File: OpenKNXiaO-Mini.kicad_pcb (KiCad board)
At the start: 4 copper layers, 23 x 30.8 mm, 13 parts, among them J1 Conn_KNX, J5 Conn_01x05, J6 Conn_01x05, J7 Conn_01x12, SW1 Prog BTN, U1 Seeeduino XIAO

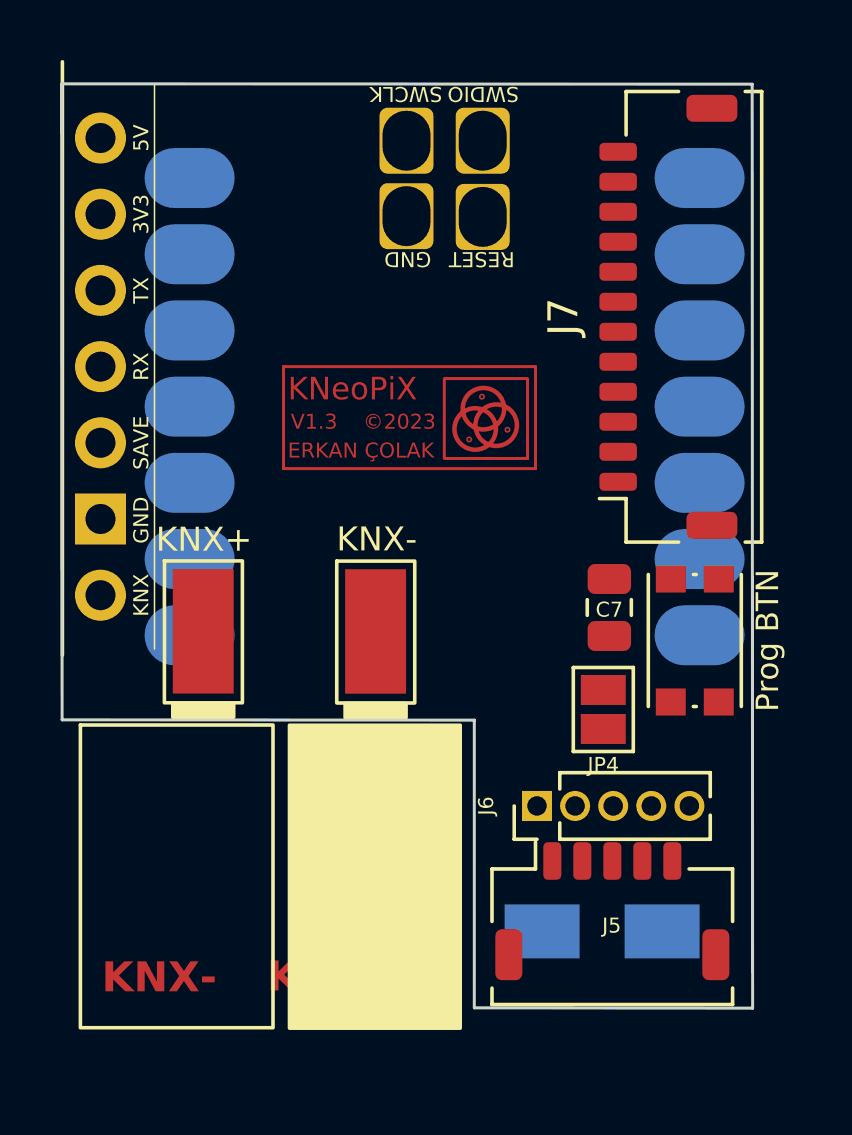
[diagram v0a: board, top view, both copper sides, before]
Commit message: OpenKNXiaO - Final form and dimensions are now established.
Initial housing is startet. Dimensions could be changed later
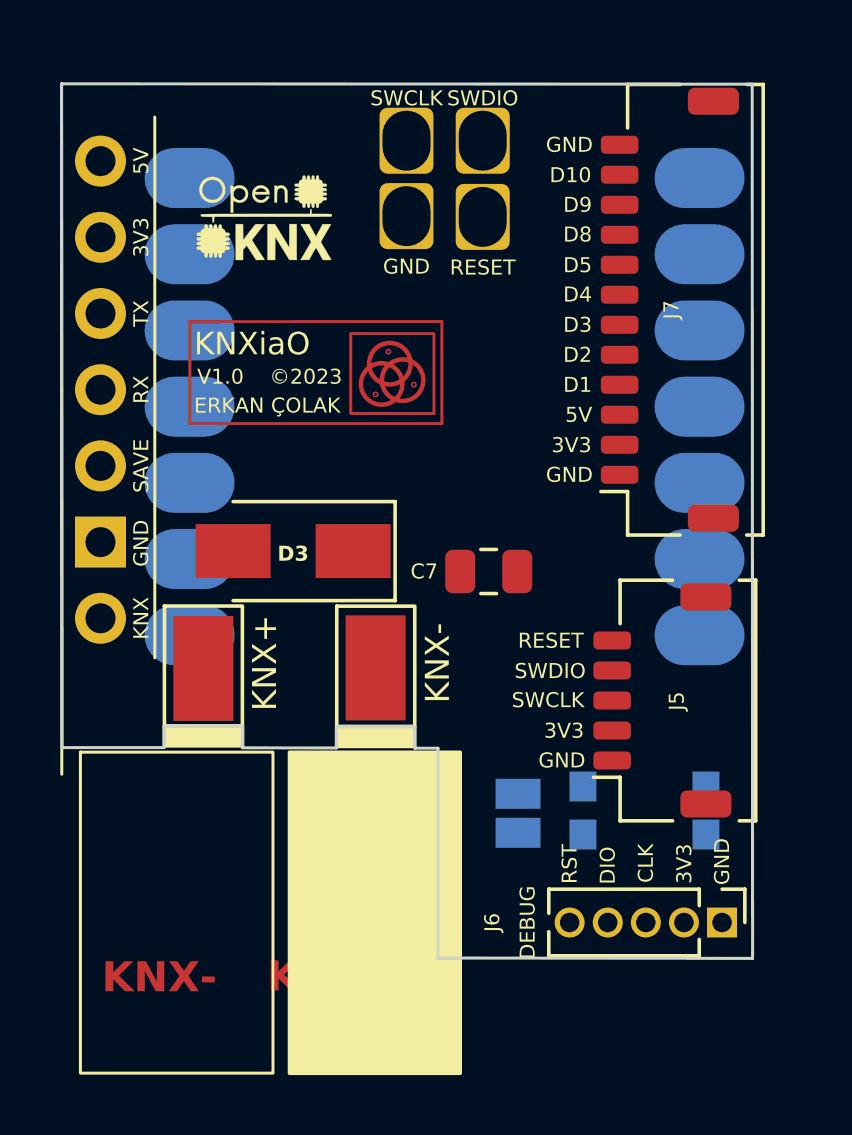
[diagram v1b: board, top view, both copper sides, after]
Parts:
- D3, REF1: moved to F.Cu
- GN1: footprint KNeoPix:NanoBCU_PinSocket_LowProfile -> KNeoPix:OpenKNX_BCU_V2.0
- JP4, SW1: moved to B.Cu
- moved REF1 21.7 mm to (118.6, 104.2), turned to 0 degrees
- moved D3 16.3 mm to (119.6, 115.1)
- moved J6 7.29 mm to (133.9, 127.5), turned to -90 degrees
- moved J5 7.22 mm to (131.9, 120.0), turned to 90 degrees
- moved SW1 5.91 mm to (131.3, 123.7), turned to 0 degrees
- moved JP4 4.48 mm to (127.1, 123.8)
- moved C7 4.20 mm to (126.1, 115.8), turned to 180 degrees
- moved REF42 3.46 mm to (120.2, 108.9)
- moved J1 1.50 mm to (116.6, 117.8)
- moved GN1 0.77 mm to (113.1, 117.3)
- moved J7 0.24 mm to (132.1, 107.0)
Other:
- board size 23 x 30.8 mm -> 23 x 29.2 mm

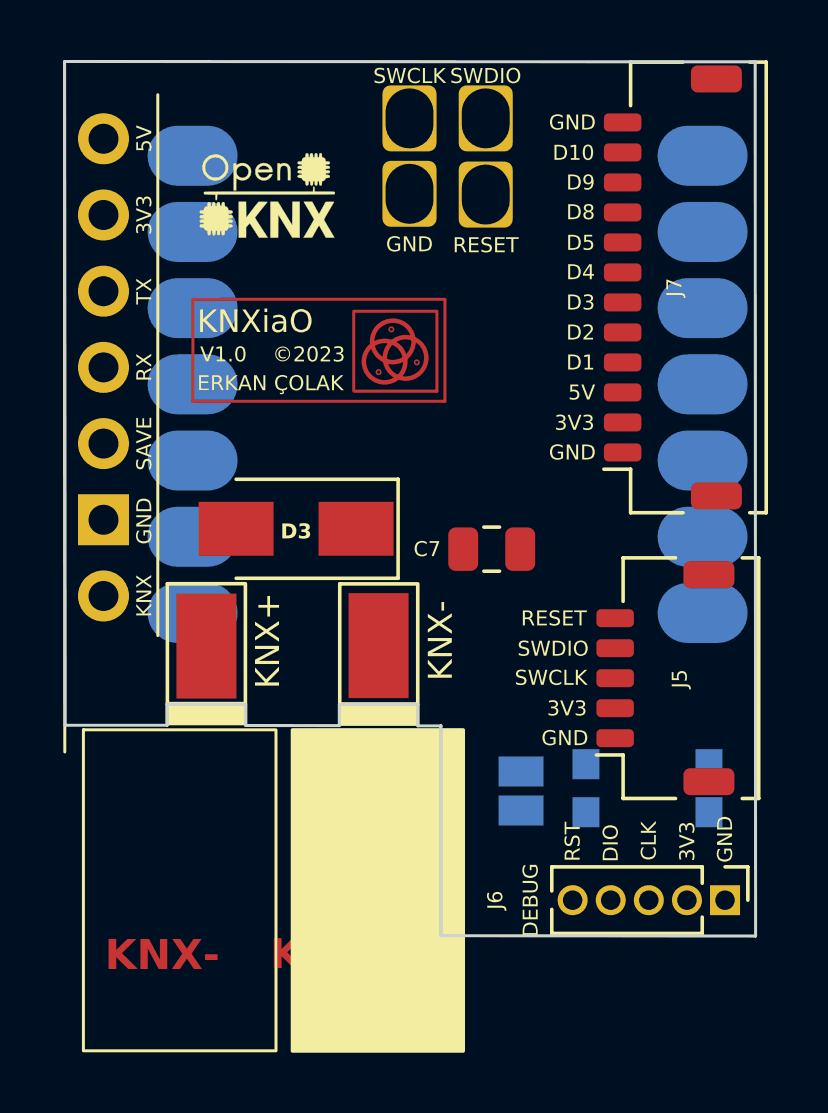
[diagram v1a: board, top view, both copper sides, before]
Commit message: Centered KNX connection and first routing
Updated low high profile (Pin-Header / Low BCU)
Removed SMA Diode. BCU has allready its own.
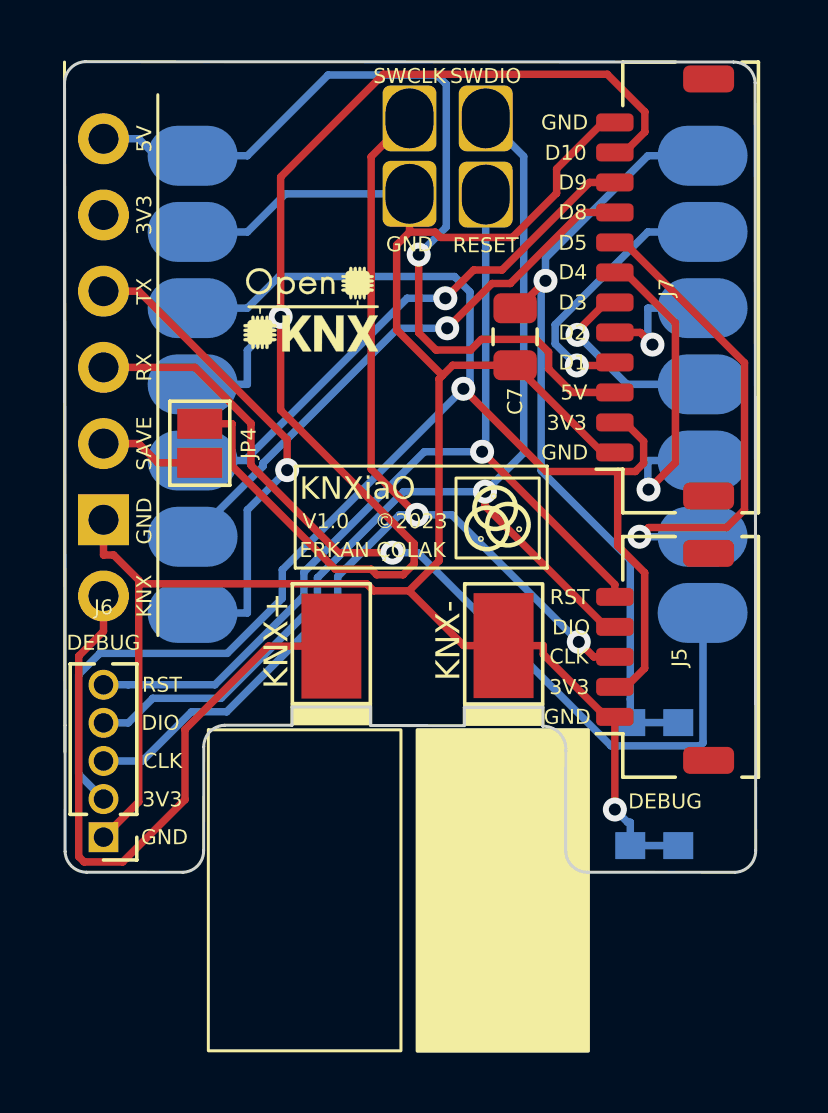
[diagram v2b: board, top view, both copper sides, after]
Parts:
- removed D3: SMAJ40CA-13-F, KNeoPix:D_SMA
- JP4: moved to F.Cu
- moved J6 20.8 mm to (113.1, 125.3), turned to 180 degrees
- moved JP4 15.8 mm to (116.3, 112.2)
- moved C7 7.12 mm to (126.9, 108.7), turned to -90 degrees
- moved REF42 6.52 mm to (123.6, 114.5)
- moved J1 4.17 mm to (120.7, 117.8)
- moved REF1 4.06 mm to (120.1, 108.0)
- moved J5 0.71 mm to (131.9, 119.3)
- moved SW1 0.27 mm to (131.5, 123.6), turned to 90 degrees
- moved J7 0.26 mm to (131.9, 107.0)
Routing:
- net KNX_GND: track 0.00 -> 74.1 mm, vias 0 -> 1
- net S_3V3: track 0.00 -> 52.4 mm, vias 0 -> 1
- net D10: track 0.00 -> 45.5 mm, vias 0 -> 1
- net SWCLK: track 0.00 -> 37.3 mm, vias 0 -> 2
- net SWDIO: track 0.00 -> 36.4 mm, vias 0 -> 1
- net RESET: track 0.00 -> 31.6 mm, vias 0 -> 1
- net KNX_RX: track 0.00 -> 30.4 mm, vias 0 -> 1
- net KNX_5V: track 0.00 -> 29.5 mm, vias 0 -> 1
- net D0: track 0.00 -> 26.4 mm, vias 0 -> 1
- net KNX+: track 0.00 -> 21.9 mm
- net D8: track 0.00 -> 18.6 mm, vias 0 -> 1
- net D9: track 0.00 -> 18.0 mm, vias 0 -> 1
- net D5_SCL: track 0.00 -> 16.9 mm, vias 0 -> 1
- net KNX_TX: track 0.00 -> 16.3 mm, vias 0 -> 1
- net D4_SDA: track 0.00 -> 11.4 mm, vias 0 -> 1
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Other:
- board size 23 x 29.2 mm -> 23 x 27 mm
- copper layers 4 -> 2
- board text removed: "KNX+"
- board text removed: "KNX-"

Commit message: Prog. Move to outside
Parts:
- moved SW1 1.80 mm to (133.3, 123.6)
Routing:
- net KNX+: track 21.9 -> 8.91 mm, vias 0 -> 1
- net KNX_RX: track 30.4 -> 25.0 mm, vias 1 -> 3
- net KNX_GND: track 74.1 -> 76.6 mm
- net RESET: track 31.6 -> 33.4 mm
- net D0: track 26.4 -> 27.8 mm
- net SWDIO: track 36.4 -> 37.7 mm
- net S_3V3: track 52.4 -> 53.7 mm, vias 1 -> 3
- net SWCLK: track 37.3 -> 38.2 mm

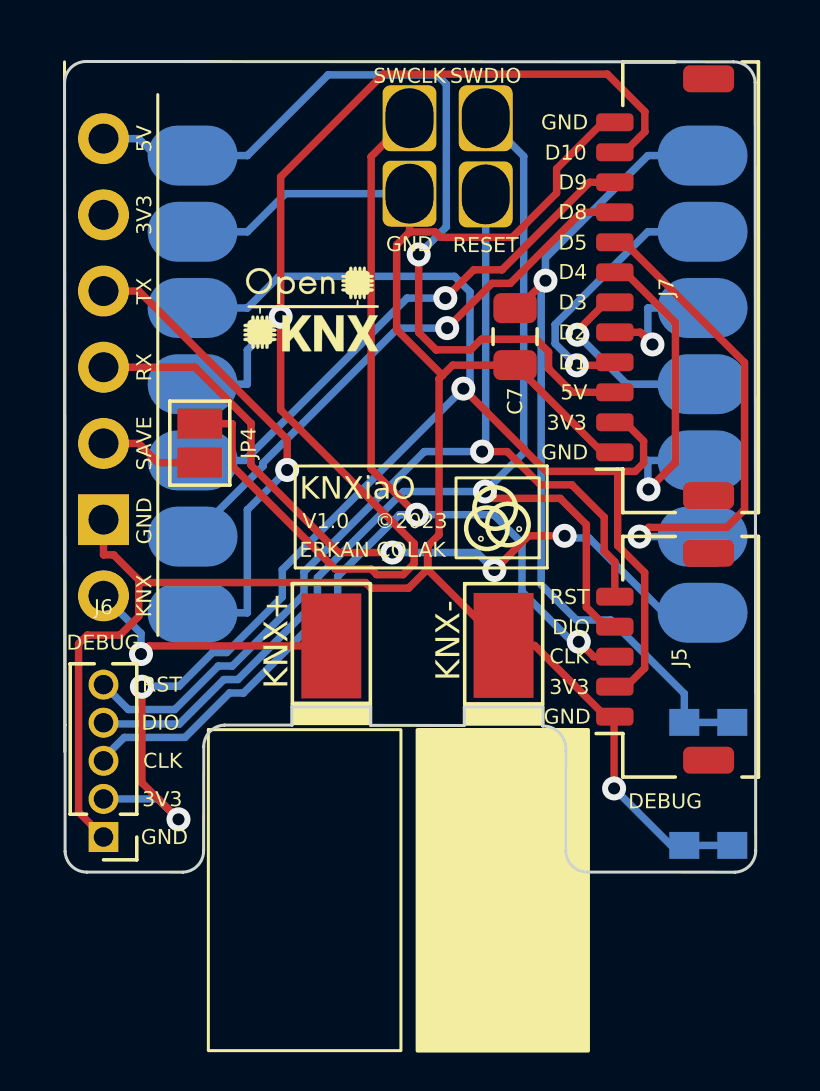
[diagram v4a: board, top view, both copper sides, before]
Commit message: rearranged Logo & Description position
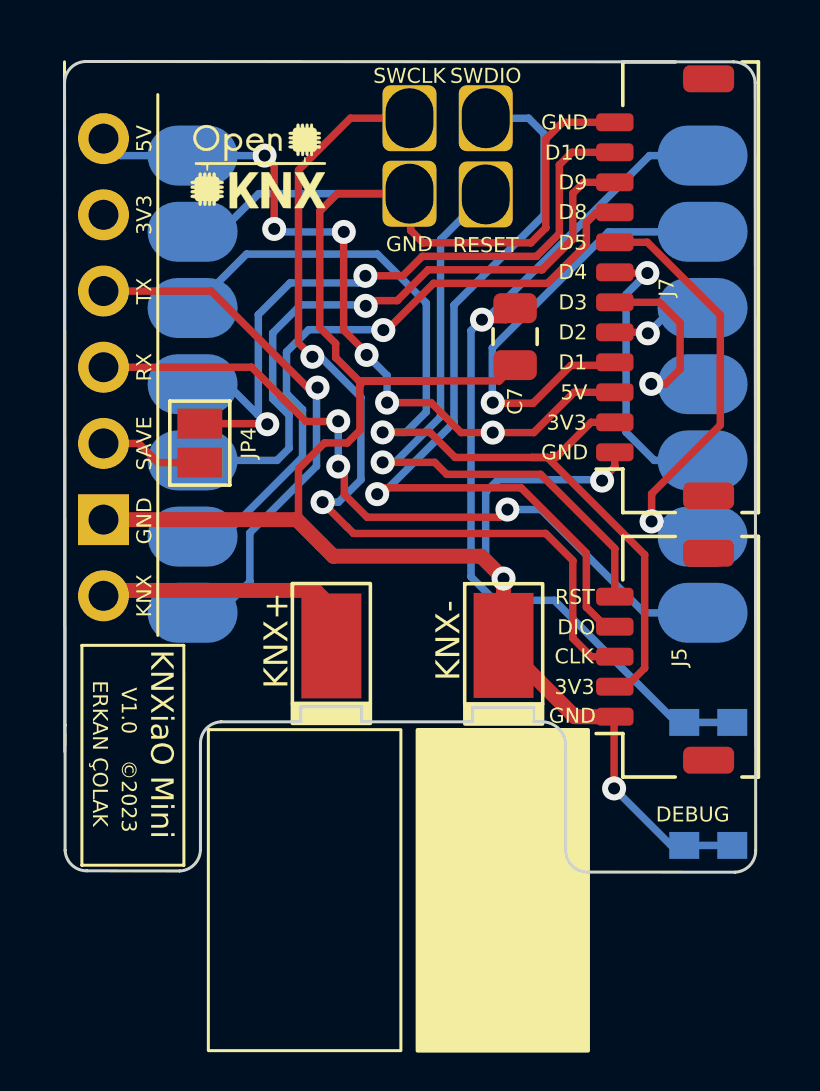
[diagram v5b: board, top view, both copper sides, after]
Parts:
- removed J6: Conn_01x05, Connector_PinHeader_1.27mm:PinHeader_1x05_P1.27mm_Vertical
- moved REF42 12.6 mm to (114.3, 123.0), turned to -90 degrees
- moved REF1 5.08 mm to (118.3, 103.2)
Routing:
- net D10: track 45.5 -> 24.6 mm, vias 1 -> 2
- net S_3V3: track 53.7 -> 32.9 mm, vias 3 -> 1
- net RESET: track 33.4 -> 21.1 mm
- net SWDIO: track 37.7 -> 27.3 mm
- net SWCLK: track 38.2 -> 30.7 mm
- net D1: track 9.17 -> 14.9 mm
- net KNX_5V: track 29.5 -> 25.4 mm, vias 1 -> 6
- net D9: track 18.0 -> 21.9 mm
- net KNX_GND: track 76.6 -> 80.2 mm, vias 1 -> 3
- net D8: track 18.6 -> 21.8 mm
- net D5_SCL: track 16.9 -> 13.9 mm
- net D0: track 27.8 -> 30.4 mm
- net D4_SDA: track 11.4 -> 9.30 mm
- net KNX_TX: track 16.3 -> 18.2 mm
- net D2: track 4.53 -> 3.29 mm
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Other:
- outline, holes or cut-outs redrawn

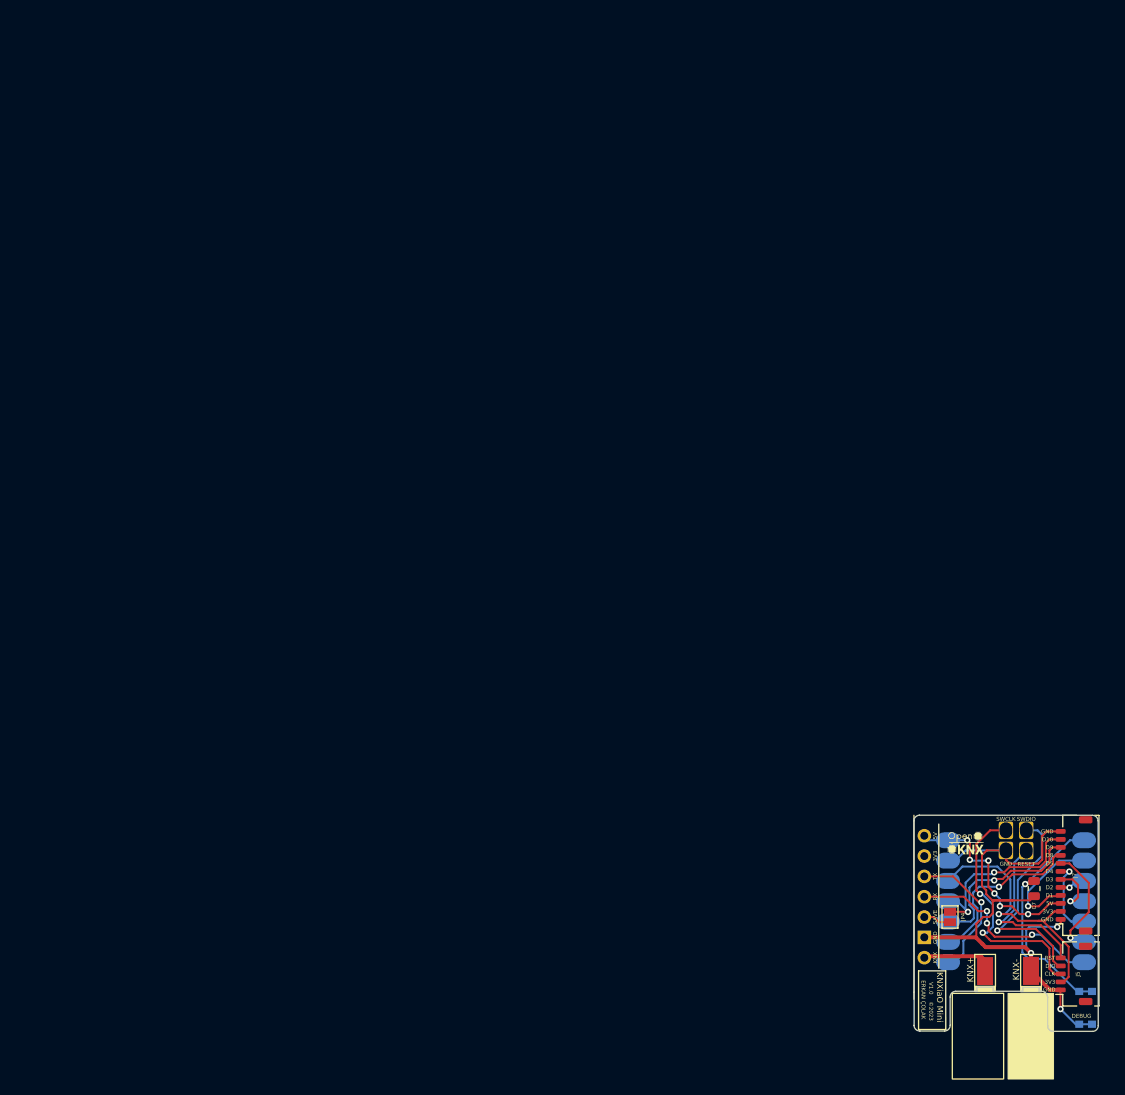
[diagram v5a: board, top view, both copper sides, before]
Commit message: Pre-Final
ToDo - Move Save <--> D10 bridge to a reachable place on the pcb
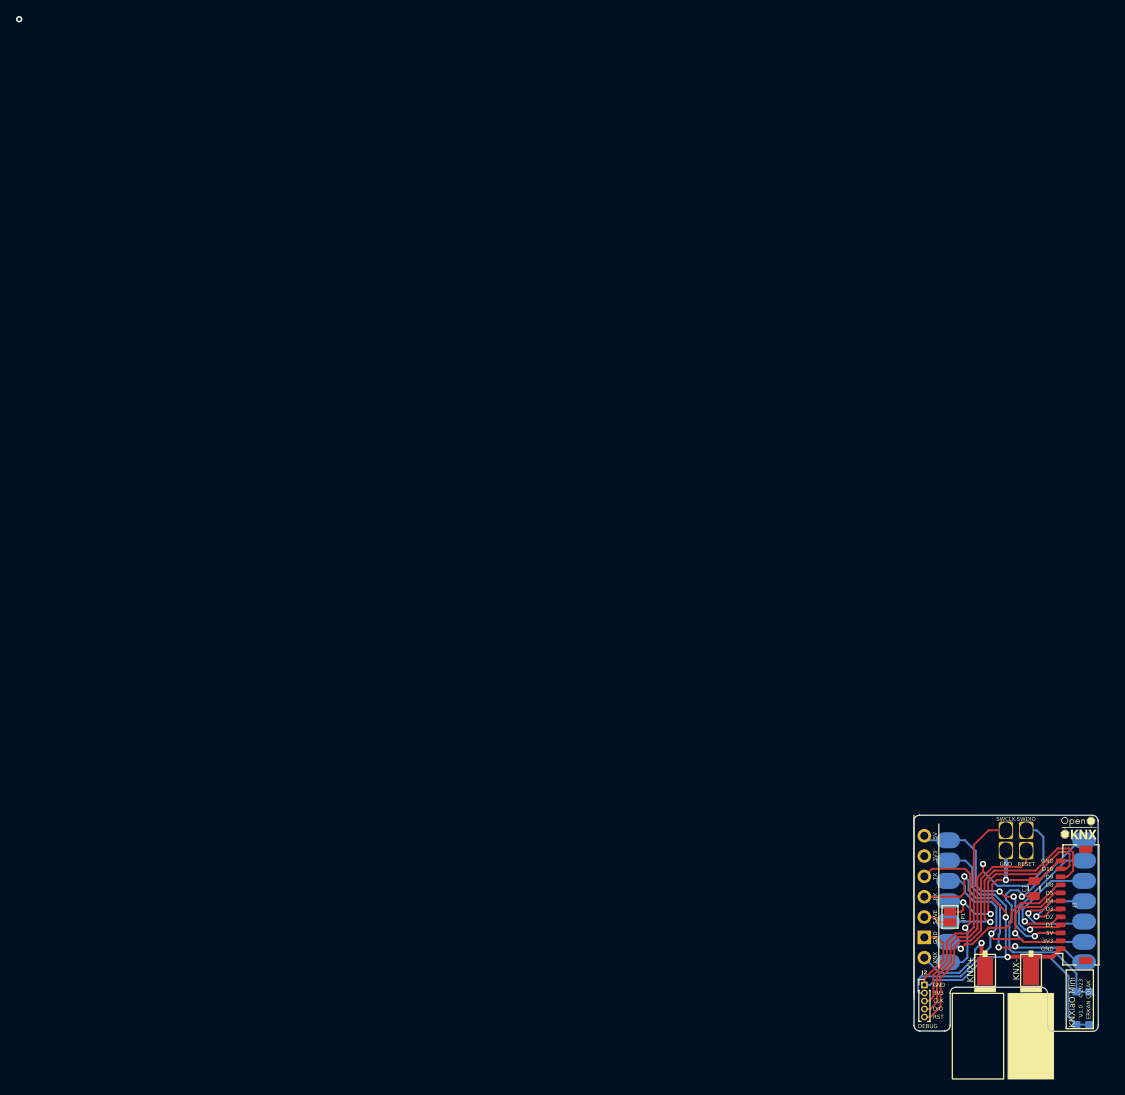
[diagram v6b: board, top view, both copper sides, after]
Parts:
- removed J5: Conn_01x05, Connector_JST:JST_SHL_SM05B-SHLS-TF_1x05-1MP_P1.00mm_Horizontal
- added J2: Conn_01x05, Connector_PinHeader_1.00mm:PinHeader_1x05_P1.00mm_Vertical, F.Cu at (113.2, 120.7)
- moved REF42 18.0 mm to (132.3, 122.1), turned to 90 degrees
- moved REF1 14.2 mm to (132.4, 101.3)
- moved J3 3.68 mm to (131.9, 110.7)
- moved REF2 3.19 mm to (124.2, 111.5), turned to 0 degrees
- moved SW1 0.35 mm to (132.9, 123.6)
- turned C1 to 90 degrees
- renumbered C7 to C1, J7 to J3, JP4 to JP1
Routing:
- net D2: track 3.29 -> 15.8 mm
- net SWDIO: track 27.3 -> 39.1 mm
- net RESET: track 21.1 -> 29.3 mm, vias 1 -> 0
- net KNX_RX: track 24.9 -> 30.8 mm
- net D9: track 21.9 -> 27.7 mm
- net D0: track 30.4 -> 35.7 mm
- net KNX+: track 9.21 -> 13.7 mm, vias 0 -> 1
- net D5_SCL: track 13.9 -> 17.9 mm
- net D8: track 21.8 -> 17.8 mm
- net D1: track 14.9 -> 18.3 mm
- net D4_SDA: track 9.30 -> 12.5 mm
- net D3: track 7.19 -> 10.3 mm
- net SWCLK: track 30.7 -> 28.1 mm, vias 2 -> 0
- net S_3V3: track 32.9 -> 35.4 mm
- net D10: track 24.6 -> 26.8 mm
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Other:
- outline, holes or cut-outs redrawn

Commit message: Final - Ready for Prototype Production.
Checked all again!
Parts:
- moved JP1 19.9 mm to (132.7, 101.0), turned to 180 degrees
- moved REF1 13.5 mm to (118.9, 101.3)
- moved REF2 1.41 mm to (124.4, 110.1), turned to 180 degrees
- moved J2 0.64 mm to (113.8, 120.8)
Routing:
- net KNX_SAVE: track 3.48 -> 30.9 mm, vias 0 -> 4
- net D10: track 26.8 -> 31.9 mm, vias 2 -> 3
- net S_3V3: track 35.4 -> 31.9 mm
- net D9: track 27.7 -> 30.2 mm
- net KNX_RX: track 30.8 -> 28.6 mm
- net D1: track 18.3 -> 19.7 mm
- net KNX_TX: track 19.9 -> 21.1 mm
- net KNX_5V: track 26.9 -> 26.2 mm
- net D8: track 17.8 -> 17.3 mm
- net KNX_GND: track 81.3 -> 80.7 mm
- net SWCLK: track 28.1 -> 27.6 mm
